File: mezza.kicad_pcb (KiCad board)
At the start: 2 copper layers, 85 x 54 mm, 19 parts, among them CON1 USB-MINI-B, P1 CONN_02X20, P2 CONN_02X20, U1 TXS0108E, U2 FT230XS, U3 CJT1117-3.3

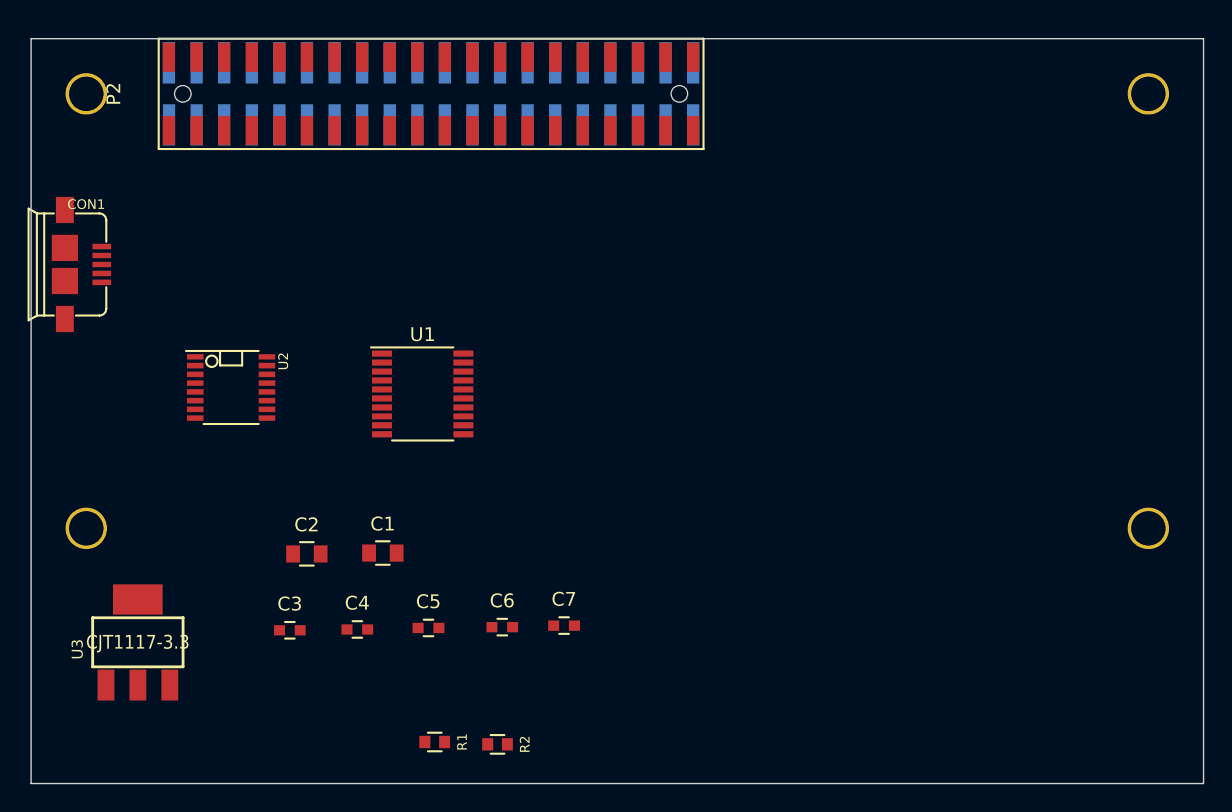
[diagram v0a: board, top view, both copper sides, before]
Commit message: Move USB Connector
USB connector has been moved to the same position as the 96Boards Sensors
board.
Components that are not connectors have been removed from the schematic.

Signed-Off-By: Sophie Haynes<sophie.haynes@linaro.org>
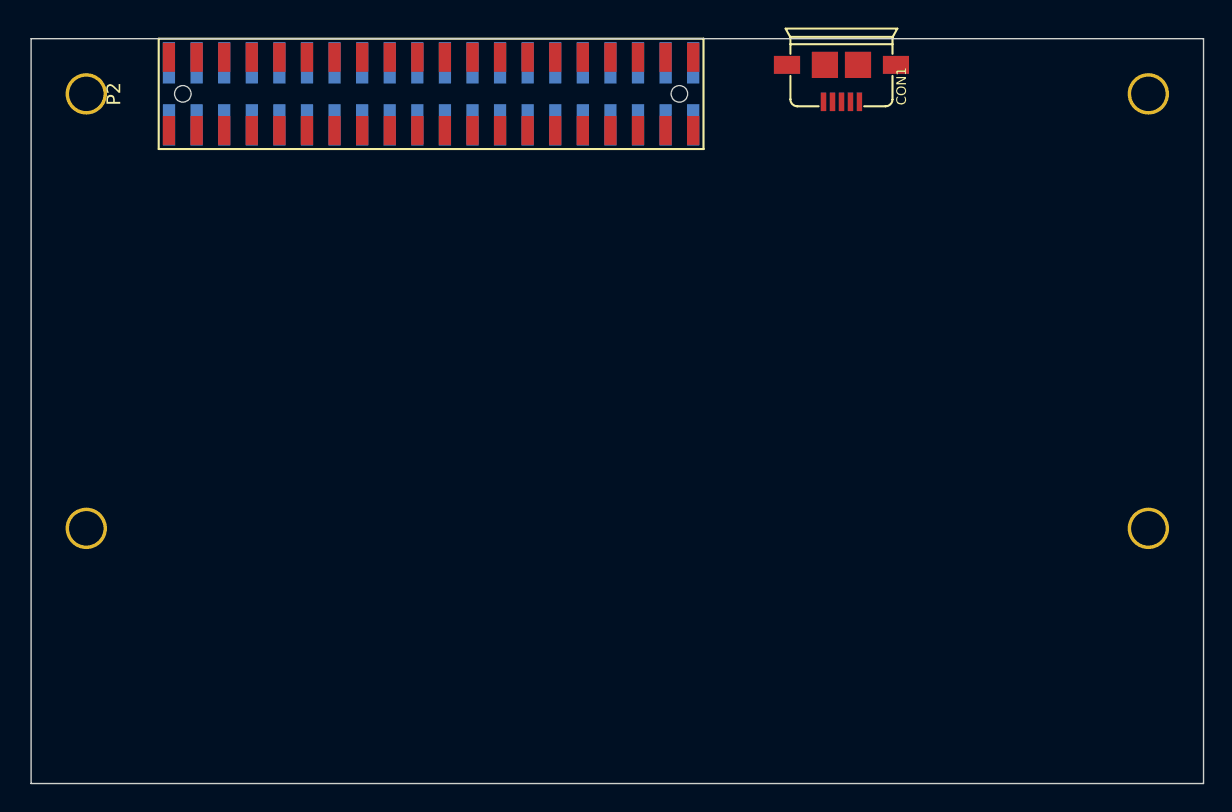
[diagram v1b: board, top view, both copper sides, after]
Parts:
- removed C1, C2: 1uF, Capacitors_SMD:C_0805
- removed C3, C7: 100nF, Capacitors_SMD:C_0603
- removed C4, C5: 39pF, Capacitors_SMD:C_0603
- removed C6: 1uF, Capacitors_SMD:C_0603
- removed R1, R2: 22R, mezza:R_0603_Seeed
- removed U1: TXS0108E, Housings_SSOP:TSSOP-20_4.4x6.5mm_Pitch0.65mm
- removed U2: FT230XS, mezza:SSOP-16_3.9x4.9mm_Pitch0.635mm_Seeed
- removed U3: CJT1117-3.3, mezza:SOT223
- moved CON1 60.0 mm to (158.8, 100.4), turned to 180 degrees
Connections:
- net GPIO-A renamed GPIO_A
- net GPIO-B renamed GPIO_B

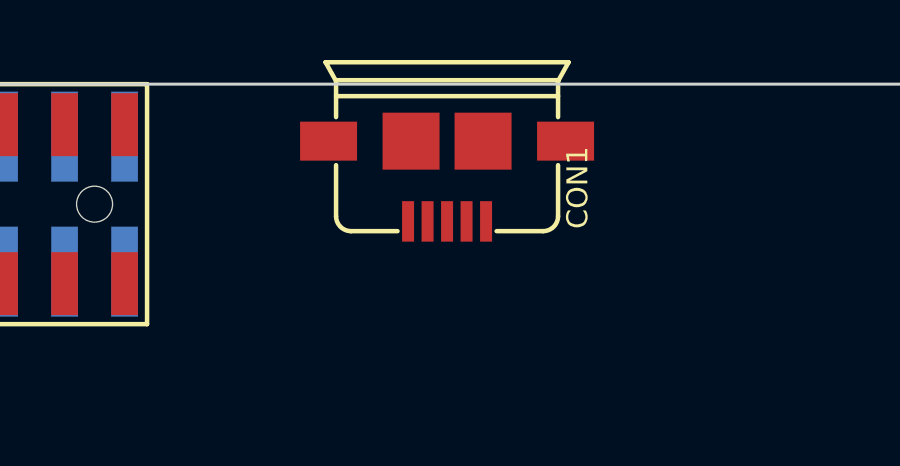
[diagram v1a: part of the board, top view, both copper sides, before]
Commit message: Tidy Up Project
Unneeded footprints have been removed from the project.
The footprint folder has been renamed (stop kicad complaining).
Readme.md has been updated to mathch the project.

Signed-off-by: Sophie Haynes <sophie.haynes@linao.org>
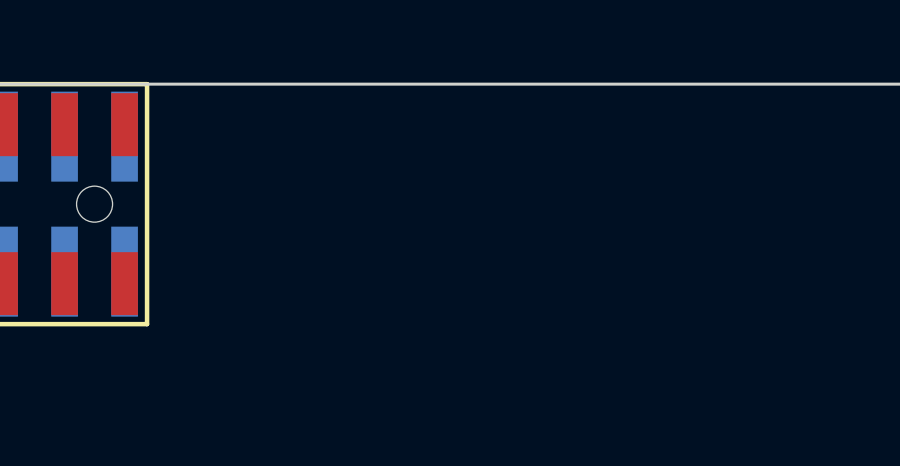
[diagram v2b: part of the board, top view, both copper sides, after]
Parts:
- removed CON1: USB-MINI-B, mezza:USB_MICRO_B_ST-USB-001E
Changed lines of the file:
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@@
 (kicad_pcb (version 4) (host pcbnew "(2015-11-19 BZR 6326)-product")
   (general
-    (links 61)
-    (no_connects 61)
-    (area 99.949999 99.949999 185.049493 154.050001)
+    (links 29)
+    (no_connects 29)
+    (area 99.366248 97.6847 185.633753 154.050001)
     (thickness 1.6)
     (drawings 4)
     (tracks 0)
     (zones 0)
-    (modules 7)
-    (nets 61)
+    (modules 6)
+    (nets 57)
   )
   (page A4)
@@
   (net 53 "Net-(P2-Pad32)")
   (net 54 "Net-(P2-Pad34)")
-  (net 55 "Net-(C4-Pad1)")
-  (net 56 "Net-(C5-Pad1)")
-  (net 57 VBUS)
-  (net 58 "Net-(CON1-Pad4)")
-  (net 59 GPIO_B)
-  (net 60 GPIO_A)
+  (net 55 GPIO_B)
+  (net 56 GPIO_A)
   (net_class Default "This is the default net class."
     (clearance 0.1778)
@@
     (uvia_dia 0.3)
     (uvia_drill 0.1)
-    (add_net +3V3)
-    (add_net +3V3_FTDI)
-    (add_net CBUS0)
-    (add_net CBUS1)
-    (add_net GPIO-A)
-    (add_net GPIO-B)
     (add_net GPIO_A)
     (add_net GPIO_B)
@@
     (add_net I2C1_SCL)
     (add_net I2C1_SDA)
-    (add_net "Net-(C1-Pad1)")
     (add_net "Net-(C4-Pad1)")
     (add_net "Net-(C5-Pad1)")
@@
     (add_net "Net-(P2-Pad34)")
     (add_net "Net-(P2-Pad8)")
-    (add_net "Net-(R1-Pad1)")
-    (add_net "Net-(R2-Pad1)")
-    (add_net "Net-(R5-Pad2)")
-    (add_net "Net-(R6-Pad2)")
-    (add_net "Net-(U1-Pad10)")
-    (add_net "Net-(U1-Pad12)")
-    (add_net "Net-(U1-Pad13)")
-    (add_net "Net-(U1-Pad14)")
-    (add_net "Net-(U1-Pad15)")
-    (add_net "Net-(U1-Pad16)")
-    (add_net "Net-(U1-Pad17)")
-    (add_net "Net-(U1-Pad18)")
-    (add_net "Net-(U1-Pad19)")
-    (add_net "Net-(U1-Pad20)")
-    (add_net "Net-(U1-Pad8)")
-    (add_net "Net-(U1-Pad9)")
-    (add_net "Net-(U2-Pad2)")
-    (add_net "Net-(U2-Pad6)")
     (add_net PWR_BTN_N)
     (add_net RST_BTN_N)
@@
       (net 7 I2C1_SDA))
     (pad 23 smd rect (at -1.65 22) (size 0.89 2.1) (layers F.Cu F.Paste F.Mask)
-      (net 60 GPIO_A))
+      (net 56 GPIO_A))
     (pad 25 smd rect (at -1.65 24) (size 0.89 2.1) (layers F.Cu F.Paste F.Mask)
       (net 37 "Net-(P2-Pad25)"))
@@
       (net 49 "Net-(P2-Pad22)"))
     (pad 24 smd rect (at 3.65 22) (size 0.89 2.1) (layers F.Cu F.Paste F.Mask)
-      (net 59 GPIO_B))
+      (net 55 GPIO_B))
     (pad 26 smd rect (at 3.65 24) (size 0.89 2.1) (layers F.Cu F.Paste F.Mask)
       (net 50 "Net-(P2-Pad26)"))
@@
       (net 18 "Net-(P1-Pad22)"))
     (pad 24 smd rect (at -3.25 -22) (size 0.89 3) (layers B.Cu B.Paste B.Mask)
-      (net 59 GPIO_B))
+      (net 55 GPIO_B))
     (pad 26 smd rect (at -3.25 -24) (size 0.89 3) (layers B.Cu B.Paste B.Mask)
       (net 19 "Net-(P1-Pad26)"))
@@
       (net 7 I2C1_SDA))
     (pad 23 smd rect (at 1.25 -22) (size 0.89 3) (layers B.Cu B.Paste B.Mask)
-      (net 60 GPIO_A))
+      (net 56 GPIO_A))
     (pad 25 smd rect (at 1.25 -24) (size 0.89 3) (layers B.Cu B.Paste B.Mask)
       (net 30 "Net-(P1-Pad25)"))
@@
     (pad 1 thru_hole circle (at 0 0) (size 3 3) (drill 2.5) (layers *.Cu *.Mask))
   )
-  (module mezza:USB_MICRO_B_ST-USB-001E (layer F.Cu)
-    (at 158.75 100.4 180)
-    (descr "USB Micro-B 5-pin SMD connector")
-    (tags "USB, Micro-B, connector")
-    (attr smd)
-    (fp_text reference CON1 (at -4.35 -3.05 270) (layer F.SilkS)
-      (effects (font (size 0.7 0.7) (thickness 0.15)))
-    )
-    (fp_text value USB-MINI-B (at 0 2 180) (layer F.SilkS) hide
-      (effects (font (size 0.5 0.5) (thickness 0.125)))
-    )
-    (fp_line (start 3.7 -0.7) (end 3.7 0.5) (layer F.SilkS) (width 0.15))
-    (fp_line (start 3.7 -4) (end 3.7 -2.3) (layer F.SilkS) (width 0.15))
-    (fp_line (start -3.7 -0.7) (end -3.7 0.5) (layer F.SilkS) (width 0.15))
-    (fp_line (start -3.7 -2.3) (end -3.7 -4) (layer F.SilkS) (width 0.15))
-    (fp_line (start 3.2 -4.5) (end 1.65 -4.5) (layer F.SilkS) (width 0.15))
-    (fp_line (start -3.2 -4.5) (end -1.65 -4.5) (layer F.SilkS) (width 0.15))
-    (fp_arc (start -3.2 -4) (end -3.7 -4) (angle 90) (layer F.SilkS) (width 0.15))
-    (fp_arc (start 3.2 -4) (end 3.2 -4.5) (angle 90) (layer F.SilkS) (width 0.15))
-    (fp_line (start -3.7 0) (end 3.7 0) (layer F.SilkS) (width 0.15))
-    (fp_line (start -3.683 0.532) (end 3.683 0.532) (layer F.SilkS) (width 0.15))
-    (fp_line (start 3.7 0.5) (end 4.05 1.13) (layer F.SilkS) (width 0.15))
-    (fp_line (start 4.05 1.13) (end -4.05 1.13) (layer F.SilkS) (width 0.15))
-    (fp_line (start -4.05 1.13) (end -3.7 0.5) (layer F.SilkS) (width 0.15))
-    (pad 4 smd rect (at 0.65 -4.175 180) (size 0.4 1.35) (layers F.Cu F.Paste F.Mask)
-      (net 58 "Net-(CON1-Pad4)"))
-    (pad 2 smd rect (at -0.65 -4.175 180) (size 0.4 1.35) (layers F.Cu F.Paste F.Mask)
-      (net 56 "Net-(C5-Pad1)"))
-    (pad 3 smd rect (at 0 -4.175 180) (size 0.4 1.35) (layers F.Cu F.Paste F.Mask)
-      (net 55 "Net-(C4-Pad1)"))
-    (pad 1 smd rect (at -1.3 -4.175 180) (size 0.4 1.35) (layers F.Cu F.Paste F.Mask)
-      (net 57 VBUS))
-    (pad 5 smd rect (at 1.3 -4.175 180) (size 0.4 1.35) (layers F.Cu F.Paste F.Mask)
-      (net 2 GND))
-    (pad 6 smd rect (at 3.95 -1.5 180) (size 1.9 1.3) (layers F.Cu F.Paste F.Mask)
-      (net 2 GND))
-    (pad 7 smd rect (at 1.2 -1.5 180) (size 1.9 1.9) (layers F.Cu F.Paste F.Mask)
-      (net 2 GND))
-    (pad 8 smd rect (at -1.2 -1.5 180) (size 1.9 1.9) (layers F.Cu F.Paste F.Mask)
-      (net 2 GND))
-    (pad 9 smd rect (at -3.95 -1.5 180) (size 1.9 1.3) (layers F.Cu F.Paste F.Mask)
-      (net 2 GND))
-  )
   (gr_line (start 100 154) (end 184.999492 154) (angle 90) (layer Edge.Cuts) (width 0.1))

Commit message: Annotate Connector in Schematic
The second connector in the schematic has been annoted to inform users who
wish to use a through hole connector instead, to delete that connector.
The correct footprints have been assigned too.

Signed-off-by: Sophie Haynes <sophie.haynes@linaro.org>
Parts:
- P1: footprint mezza:Socket_Strip_SMD_2x20_Pitch2mm -> 96boards:Socket_Strip_SMD_2x20_Pitch2mm
- P2: footprint mezza:Pin_Header_SMD_2x20_Pitch2mm -> 96boards:Pin_Header_SMD_2x20_Pitch2mm
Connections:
- P1 pad 10: Net-(P1-Pad10) -> SPIO_DIN
- P1 pad 11: Net-(P1-Pad11) -> UART1_TX
- P1 pad 12: Net-(P1-Pad12) -> SPIO_CS
- P1 pad 13: Net-(P1-Pad13) -> UART1_RX
- P1 pad 14: Net-(P1-Pad14) -> SPIO_DOUT
- P1 pad 16: Net-(P1-Pad16) -> PCM_FS
- P1 pad 18: Net-(P1-Pad18) -> PCM_CLK
- P1 pad 20: Net-(P1-Pad20) -> PCM_DO
- P1 pad 22: Net-(P1-Pad22) -> PCM_DI
- P1 pad 25: Net-(P1-Pad25) -> GPIO_C
- P1 pad 26: Net-(P1-Pad26) -> GPIO_D
- P1 pad 27: Net-(P1-Pad27) -> GPIO_E
- P1 pad 28: Net-(P1-Pad28) -> GPIO_F
- P1 pad 29: Net-(P1-Pad29) -> GPIO_G
- P1 pad 3: UART_CTS -> (no net)
- P1 pad 30: Net-(P1-Pad30) -> GPIO_H
- P1 pad 31: Net-(P1-Pad31) -> GPIO_I
- P1 pad 32: Net-(P1-Pad32) -> GPIO_J
- P1 pad 33: Net-(P1-Pad33) -> GPIO_K
- P1 pad 34: Net-(P1-Pad34) -> GPIO_L
- P1 pad 5: UART_TX -> (no net)
- P1 pad 7: UART_RX -> (no net)
- P1 pad 8: Net-(P1-Pad8) -> SPIO_SCL
- P1 pad 9: UART_RTS -> (no net)
- P2 pad 10: Net-(P2-Pad10) -> SPIO_DIN
- P2 pad 11: Net-(P2-Pad11) -> UART1_TX
- P2 pad 12: Net-(P2-Pad12) -> SPIO_CS
- P2 pad 13: Net-(P2-Pad13) -> UART1_RX
- P2 pad 14: Net-(P2-Pad14) -> SPIO_DOUT
- P2 pad 16: Net-(P2-Pad16) -> PCM_FS
- P2 pad 18: Net-(P2-Pad18) -> PCM_CLK
- P2 pad 20: Net-(P2-Pad20) -> PCM_DO
- P2 pad 22: Net-(P2-Pad22) -> PCM_DI
- P2 pad 25: Net-(P2-Pad25) -> GPIO_C
- P2 pad 26: Net-(P2-Pad26) -> GPIO_D
- P2 pad 27: Net-(P2-Pad27) -> GPIO_E
- P2 pad 28: Net-(P2-Pad28) -> GPIO_F
- P2 pad 29: Net-(P2-Pad29) -> GPIO_G
- P2 pad 3: UART_CTS -> (no net)
- P2 pad 30: Net-(P2-Pad30) -> GPIO_H
- P2 pad 31: Net-(P2-Pad31) -> GPIO_I
- P2 pad 32: Net-(P2-Pad32) -> GPIO_J
- P2 pad 33: Net-(P2-Pad33) -> GPIO_K
- P2 pad 34: Net-(P2-Pad34) -> GPIO_L
- P2 pad 5: UART_TX -> (no net)
- P2 pad 7: UART_RX -> (no net)
- P2 pad 8: Net-(P2-Pad8) -> SPIO_SCL
- P2 pad 9: UART_RTS -> (no net)

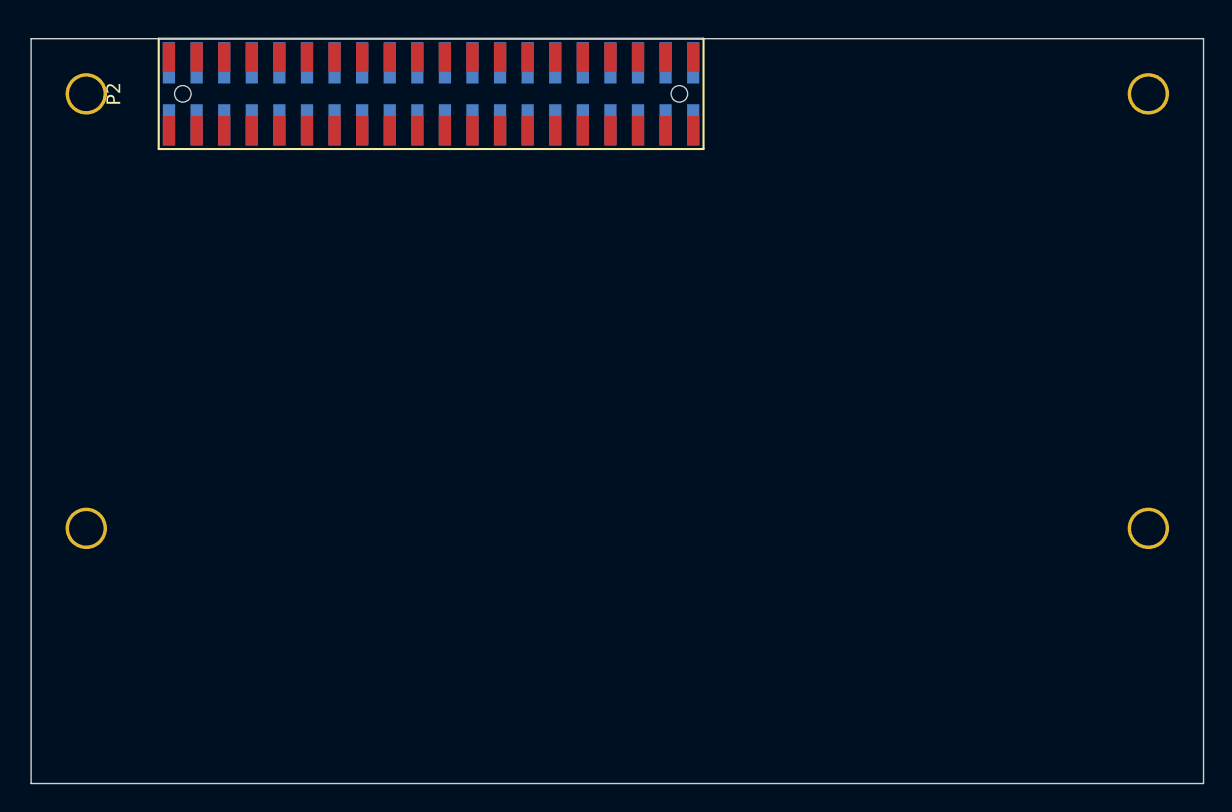
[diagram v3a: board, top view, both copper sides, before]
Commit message: Fix Pad Placement For Mounting Holes
With all the changes made over time, two of the mounting holes
has shifted slightly out of place. This has been rectifed.

Signed-off-by: Sophie Haynes <sophie.haynes@linaro.org>
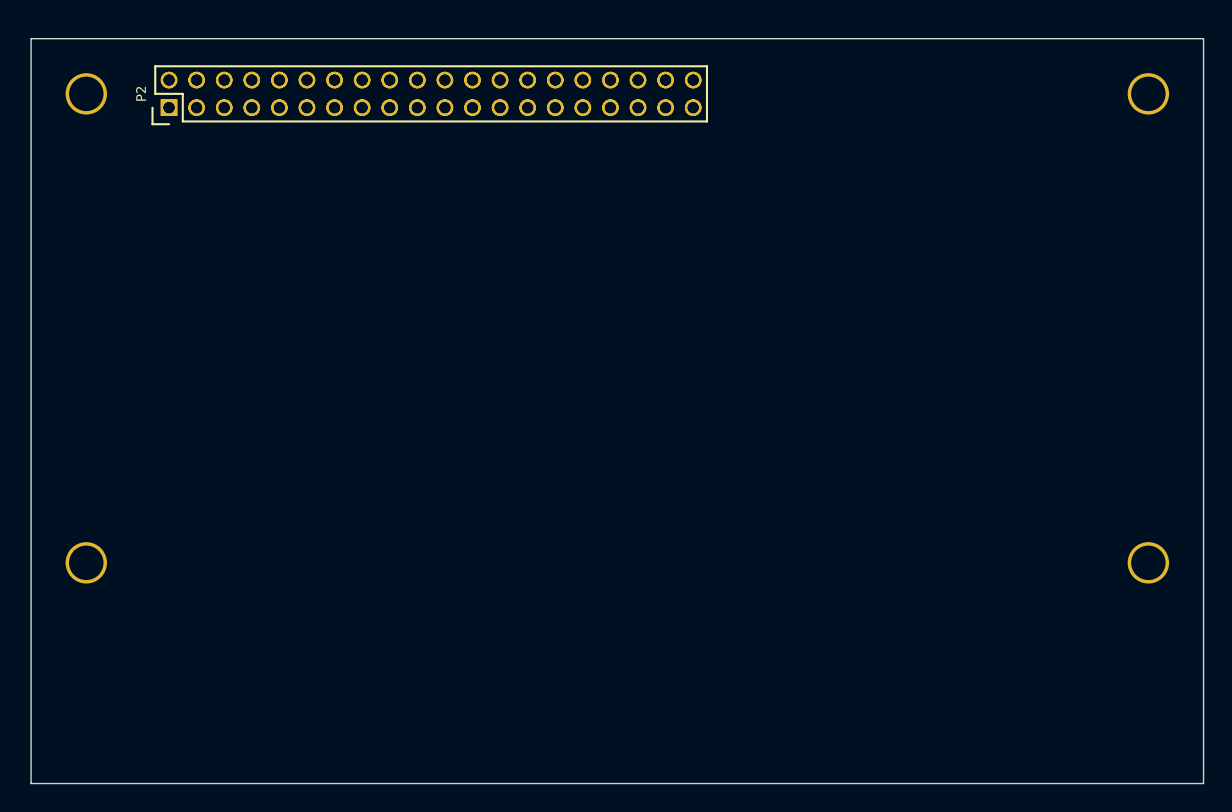
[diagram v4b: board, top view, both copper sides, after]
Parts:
- P1: footprint 96boards:Socket_Strip_SMD_2x20_Pitch2mm -> 96boards:Pin_Header_Straight_2x20_Pitch2mm
- P2: footprint 96boards:Pin_Header_SMD_2x20_Pitch2mm -> 96boards:Socket_Strip_Straight_2x20_Pitch2mm
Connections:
- P1 pad 3: (no net) -> UART0_CTS
- P1 pad 5: (no net) -> UART0_TX
- P1 pad 7: (no net) -> UART0_RX
- P1 pad 9: (no net) -> UART0_RTS
- P2 pad 3: (no net) -> UART0_CTS
- P2 pad 5: (no net) -> UART0_TX
- P2 pad 7: (no net) -> UART0_RX
- P2 pad 9: (no net) -> UART0_RTS
